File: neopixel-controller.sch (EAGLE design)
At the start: 22 parts, among them Q1 BSS138, Q2 BSS138, U1 ESP-WROOM-02, U2 AP2112K

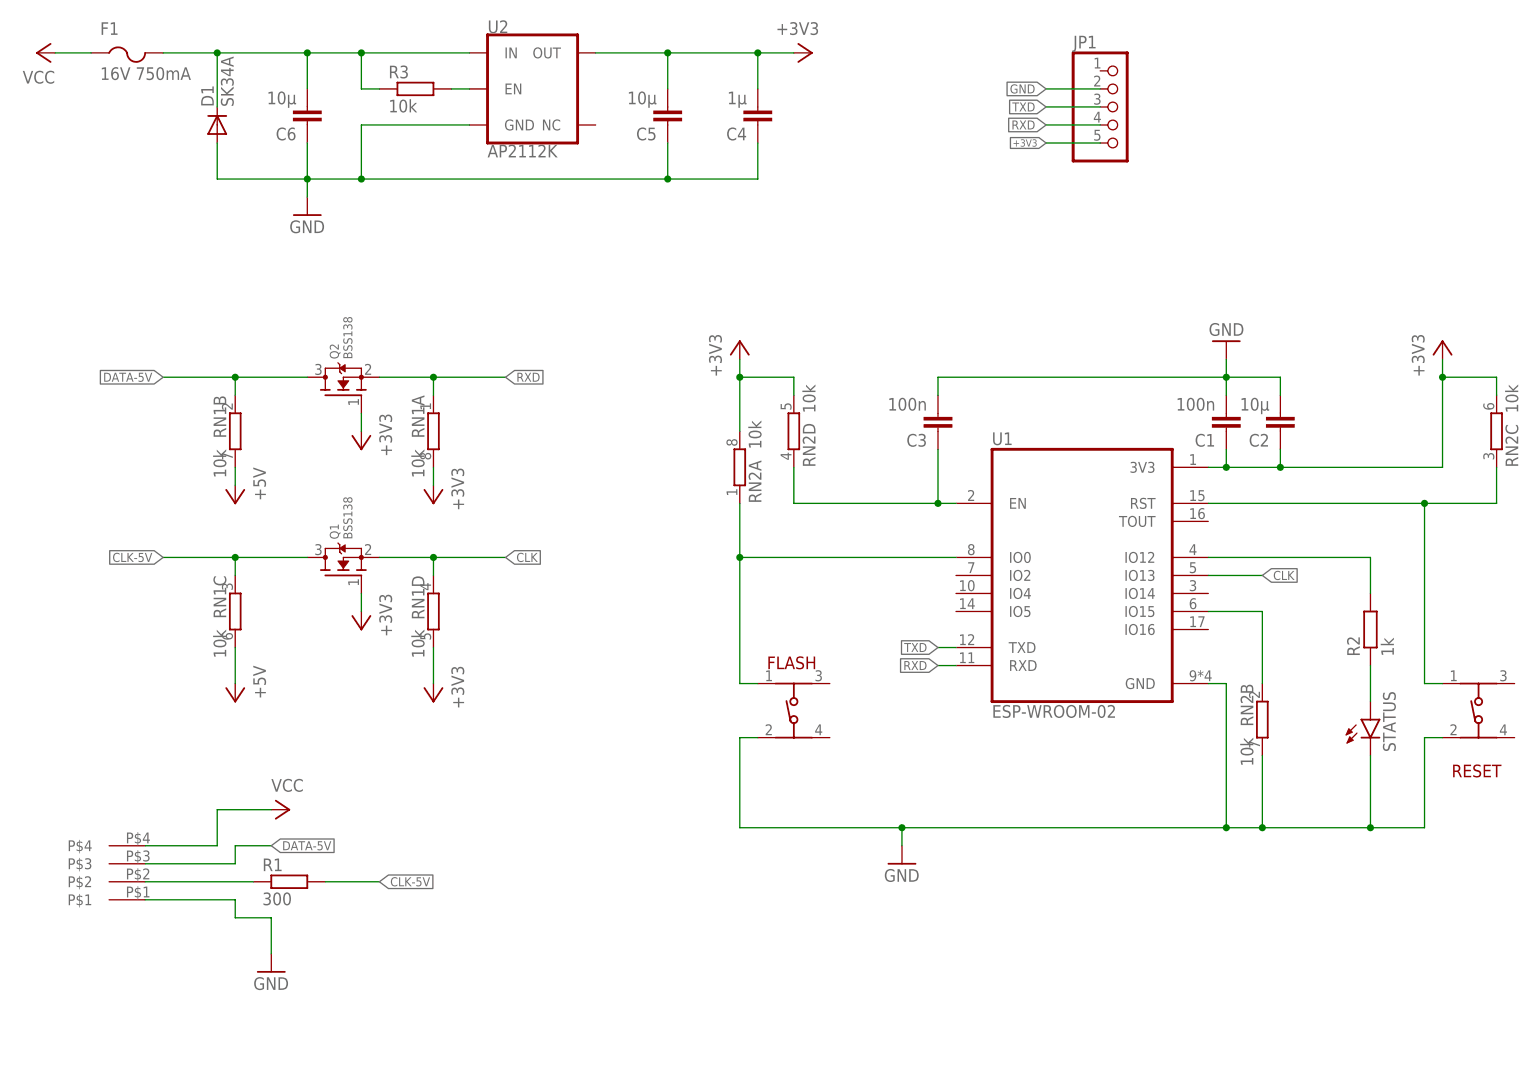
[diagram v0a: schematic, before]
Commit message: added 74ahct125, rework for v0.5
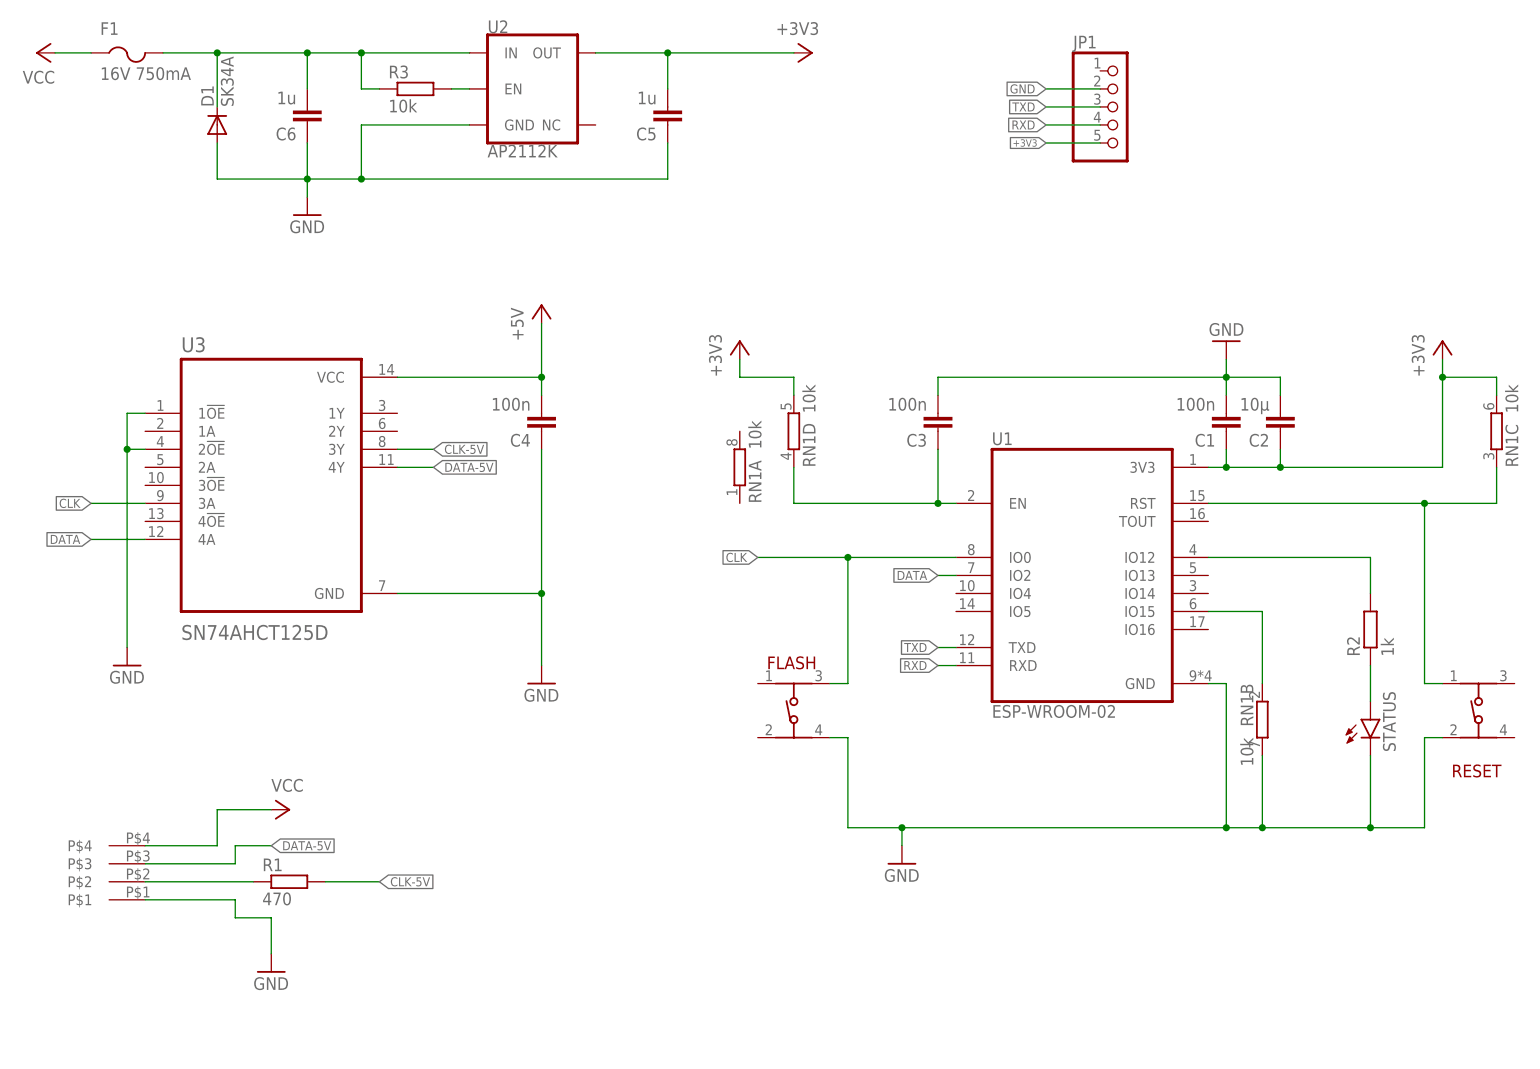
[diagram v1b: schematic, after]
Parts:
- removed Q1, Q2: BSS138, adafruit:MOSFET-NREFLOW
- removed RN2: 10k, resistor-dil:4R-NEXB38V
- added U3: SN74AHCT125D, SN74AHCT125D:SN74AHCT125D
- C4: value 1µ -> 100n
- C5, C6: value 10µ -> 1u
- R1: value 300 -> 470
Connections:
- removed net FLASH: FLASH.1, RN2A.1, U1.IO0
- new net DATA: U1.IO2, U3.4A
- net +3V3: now also RN1C.2; no longer C4.2, Q1.G, Q2.G, RN1A.2, RN2A.2, RN2C.2, RN2D.2
- net +5V: now also C4.2, U3.VCC; no longer RN1B.2, RN1C.2
- net BOOTMODE: now also RN1B.1; no longer RN2B.1
- net CHIPEN: now also RN1D.1; no longer RN2D.1
- net CLK: now also FLASH.2, U1.IO0, U3.3A; no longer Q1.S, RN1D.1, U1.IO13
- net CLK-5V: now also U3.3Y; no longer Q1.D, RN1C.1
- net DATA-5V: now also U3.4Y; no longer Q2.D, RN1B.1
- net GND: now also FLASH.4, RN1B.2, U3.1!OE, U3.2!OE, U3.GND; no longer FLASH.3, RN2B.2
- net RST: now also RN1C.1; no longer RN2C.1
- net RXD: no longer Q2.S, RN1A.1
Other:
- moved on the sheet: C4, RN1A, RN1B, RN1C, RN1D

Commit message: v0.5 pr
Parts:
- F1: value 16V 750mA -> 8V 500mA
- R1: value 470 -> 330
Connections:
- removed net N$3: R1.1, U$101.P$2
- new net DATA-5VR: R1.1, U$101.P$3
- net CLK-5V: now also U$101.P$2; no longer R1.2
- net DATA-5V: now also R1.2; no longer U$101.P$3
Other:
- moved on the sheet: R1
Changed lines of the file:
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@@
 <part name="JP1" library="pinhead" library_urn="urn:adsk.eagle:library:325" deviceset="PINHD-1X5" device="" package3d_urn="urn:adsk.eagle:package:22469/2"/>
 <part name="GND1" library="supply1" deviceset="GND" device=""/>
-<part name="R1" library="rcl" library_urn="urn:adsk.eagle:library:334" deviceset="R-EU_" device="R0805" package3d_urn="urn:adsk.eagle:package:23553/2" value="470"/>
+<part name="R1" library="rcl" library_urn="urn:adsk.eagle:library:334" deviceset="R-EU_" device="R0805" package3d_urn="urn:adsk.eagle:package:23553/2" value="330"/>
 <part name="FRAME1" library="frames" library_urn="urn:adsk.eagle:library:229" deviceset="A4L-LOC" device=""/>
 <part name="FLASH" library="434153017835_Eagle_WS-TASV_rev20a" deviceset="434153017835" device="" package3d_urn="urn:adsk.eagle:package:18304352/2"/>
@@
 <part name="D1" library="diode" library_urn="urn:adsk.eagle:library:210" deviceset="DIODE-" device="DO214AC" package3d_urn="urn:adsk.eagle:package:43417/2" value="SK34A"/>
 <part name="P+1" library="supply1" library_urn="urn:adsk.eagle:library:371" deviceset="VCC" device=""/>
-<part name="F1" library="adafruit" library_urn="urn:adsk.eagle:library:420" deviceset="PTCFUSE" device="-1206" package3d_urn="urn:adsk.eagle:package:6240569/1" override_package3d_urn="urn:adsk.eagle:package:20945049/2" override_package_urn="urn:adsk.eagle:footprint:6239923/1" value="16V 750mA"/>
+<part name="F1" library="adafruit" library_urn="urn:adsk.eagle:library:420" deviceset="PTCFUSE" device="-1206" package3d_urn="urn:adsk.eagle:package:6240569/1" override_package3d_urn="urn:adsk.eagle:package:20945049/2" override_package_urn="urn:adsk.eagle:footprint:6239923/1" value="8V 500mA"/>
 <part name="RN1" library="resistor-dil" library_urn="urn:adsk.eagle:library:342" deviceset="4R-N" device="EXB38V" package3d_urn="urn:adsk.eagle:package:24923/1" override_package3d_urn="urn:adsk.eagle:package:20945039/2" override_package_urn="urn:adsk.eagle:footprint:24902/1" value="10k"/>
 <part name="U3" library="SN74AHCT125D" deviceset="SN74AHCT125D" device="" override_package3d_urn="urn:adsk.eagle:package:23111573/2" override_package_urn="urn:adsk.eagle:footprint:23111574/1"/>
@@
 <attribute name="VALUE" x="149.86" y="35.56" size="1.778" layer="96"/>
 </instance>
-<instance part="+3V35" gate="G$1" x="129.54" y="111.76" smashed="yes">
-<attribute name="VALUE" x="127" y="106.68" size="1.778" layer="96" rot="R90"/>
+<instance part="+3V35" gate="G$1" x="137.16" y="111.76" smashed="yes">
+<attribute name="VALUE" x="134.62" y="106.68" size="1.778" layer="96" rot="R90"/>
 </instance>
 <instance part="+3V37" gate="G$1" x="228.6" y="111.76" smashed="yes">
@@
 <attribute name="VALUE" x="60.96" y="20.32" size="1.778" layer="96"/>
 </instance>
-<instance part="R1" gate="G$1" x="66.04" y="35.56" smashed="yes">
-<attribute name="NAME" x="62.23" y="37.0586" size="1.778" layer="95"/>
-<attribute name="VALUE" x="62.23" y="32.258" size="1.778" layer="96"/>
+<instance part="R1" gate="G$1" x="68.58" y="40.64" smashed="yes">
+<attribute name="NAME" x="64.77" y="42.1386" size="1.778" layer="95"/>
+<attribute name="VALUE" x="64.77" y="37.338" size="1.778" layer="96"/>
 </instance>
 <instance part="FRAME1" gate="G$1" x="0" y="0" smashed="yes">
@@
 <segment>
 <pinref part="+3V35" gate="G$1" pin="+3V3"/>
-<wire x1="129.54" y1="106.68" x2="129.54" y2="109.22" width="0.1524" layer="91"/>
-<wire x1="137.16" y1="104.14" x2="137.16" y2="106.68" width="0.1524" layer="91"/>
-<wire x1="137.16" y1="106.68" x2="129.54" y2="106.68" width="0.1524" layer="91"/>
+<wire x1="137.16" y1="104.14" x2="137.16" y2="109.22" width="0.1524" layer="91"/>
 <pinref part="RN1" gate="D" pin="2"/>
 </segment>
@@
 <net name="DATA-5V" class="0">
 <segment>
-<wire x1="58.42" y1="40.64" x2="63.5" y2="40.64" width="0.1524" layer="91"/>
-<label x="63.5" y="40.64" size="1.27" layer="95" xref="yes"/>
-<pinref part="U$101" gate="G$1" pin="P$3"/>
-<wire x1="45.72" y1="38.1" x2="58.42" y2="38.1" width="0.1524" layer="91"/>
-<wire x1="58.42" y1="38.1" x2="58.42" y2="40.64" width="0.1524" layer="91"/>
-</segment>
-<segment>
 <label x="86.36" y="93.98" size="1.27" layer="95" xref="yes"/>
 <pinref part="U3" gate="G$1" pin="4Y"/>
 <wire x1="81.28" y1="93.98" x2="86.36" y2="93.98" width="0.1524" layer="91"/>
+</segment>
+<segment>
+<wire x1="73.66" y1="40.64" x2="78.74" y2="40.64" width="0.1524" layer="91"/>
+<label x="78.74" y="40.64" size="1.27" layer="95" xref="yes"/>
+<pinref part="R1" gate="G$1" pin="2"/>
 </segment>
 </net>
@@
 </segment>
 <segment>
-<pinref part="R1" gate="G$1" pin="2"/>
-<wire x1="71.12" y1="35.56" x2="78.74" y2="35.56" width="0.1524" layer="91"/>
-<label x="78.74" y="35.56" size="1.27" layer="95" xref="yes"/>
+<label x="76.2" y="35.56" size="1.27" layer="95" xref="yes"/>
+<pinref part="U$101" gate="G$1" pin="P$2"/>
+<wire x1="45.72" y1="35.56" x2="76.2" y2="35.56" width="0.1524" layer="91"/>
 </segment>
 </net>
@@
 </segment>
 </net>
-<net name="N$3" class="0">
-<segment>
-<pinref part="U$101" gate="G$1" pin="P$2"/>
-<pinref part="R1" gate="G$1" pin="1"/>
-<wire x1="45.72" y1="35.56" x2="60.96" y2="35.56" width="0.1524" layer="91"/>
-</segment>
-</net>
 <net name="DATA" class="0">
 <segment>
@@
 </segment>
 </net>
+<net name="DATA-5VR" class="0">
+<segment>
+<pinref part="U$101" gate="G$1" pin="P$3"/>
+<wire x1="45.72" y1="38.1" x2="60.96" y2="38.1" width="0.1524" layer="91"/>
+<wire x1="60.96" y1="38.1" x2="60.96" y2="40.64" width="0.1524" layer="91"/>
+<pinref part="R1" gate="G$1" pin="1"/>
+<wire x1="60.96" y1="40.64" x2="63.5" y2="40.64" width="0.1524" layer="91"/>
+</segment>
+</net>

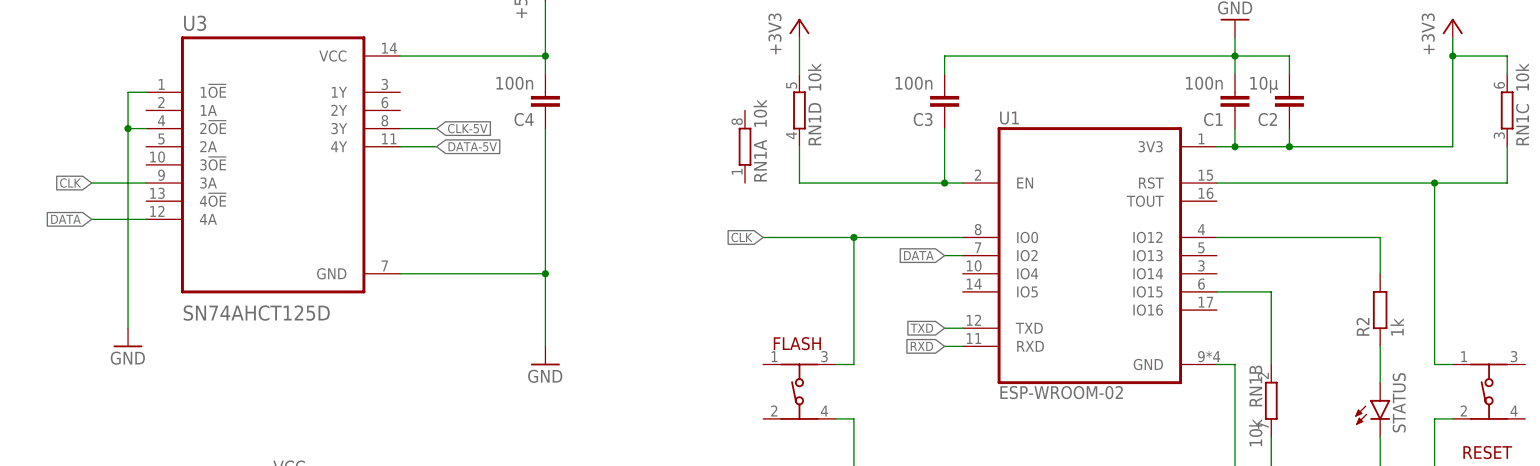
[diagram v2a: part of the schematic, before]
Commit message: fixed OE of 74AHCT125
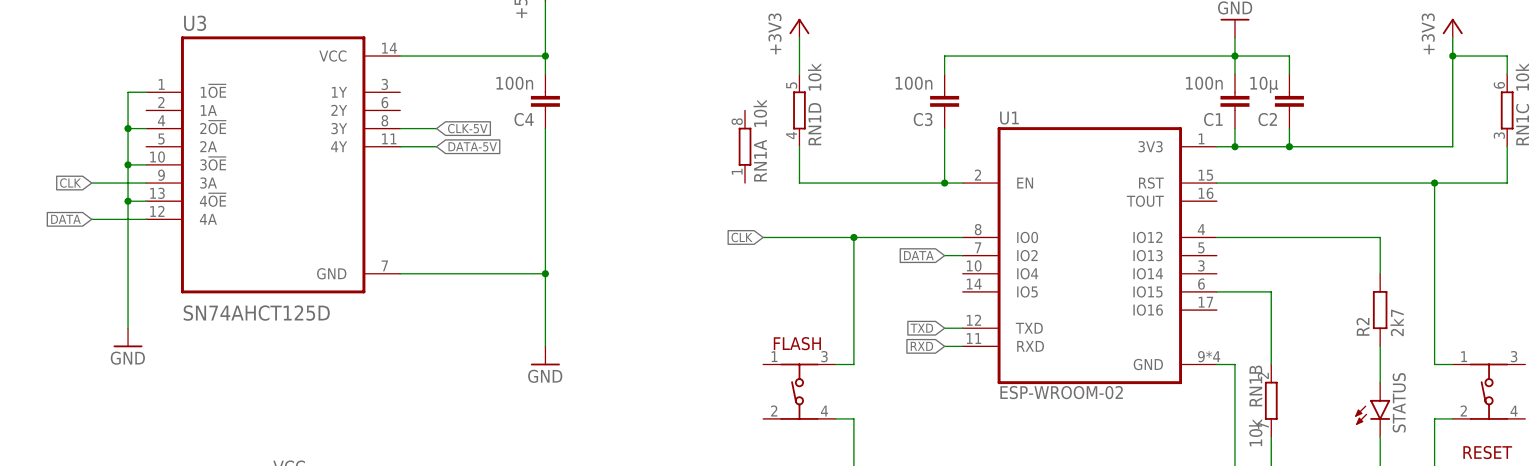
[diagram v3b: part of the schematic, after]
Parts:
- R2: value 1k -> 2k7
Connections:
- net GND: now also U3.3!OE, U3.4!OE
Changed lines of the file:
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@@
 <part name="C3" library="rcl" library_urn="urn:adsk.eagle:library:334" deviceset="C-EU" device="C0805" package3d_urn="urn:adsk.eagle:package:23617/2" value="100n"/>
 <part name="U1" library="ESP-WROOM-02" deviceset="ESP-WROOM-02" device="" override_package3d_urn="urn:adsk.eagle:package:14797501/2" override_package_urn="urn:adsk.eagle:footprint:14797502/1" override_locally_modified="yes"/>
-<part name="R2" library="rcl" library_urn="urn:adsk.eagle:library:334" deviceset="R-EU_" device="R0805" package3d_urn="urn:adsk.eagle:package:23553/2" value="1k"/>
+<part name="R2" library="rcl" library_urn="urn:adsk.eagle:library:334" deviceset="R-EU_" device="R0805" package3d_urn="urn:adsk.eagle:package:23553/2" value="2k7"/>
 <part name="STATUS" library="led" library_urn="urn:adsk.eagle:library:259" deviceset="LED" device="CHIPLED_0805" package3d_urn="urn:adsk.eagle:package:15821/2"/>
 <part name="JP1" library="pinhead" library_urn="urn:adsk.eagle:library:325" deviceset="PINHD-1X5" device="" package3d_urn="urn:adsk.eagle:package:22469/2"/>
@@
 <wire x1="43.18" y1="101.6" x2="43.18" y2="96.52" width="0.1524" layer="91"/>
 <pinref part="U3" gate="G$1" pin="2!OE"/>
-<wire x1="43.18" y1="96.52" x2="43.18" y2="68.58" width="0.1524" layer="91"/>
+<wire x1="43.18" y1="96.52" x2="43.18" y2="91.44" width="0.1524" layer="91"/>
+<wire x1="43.18" y1="91.44" x2="43.18" y2="86.36" width="0.1524" layer="91"/>
+<wire x1="43.18" y1="86.36" x2="43.18" y2="68.58" width="0.1524" layer="91"/>
 <wire x1="45.72" y1="96.52" x2="43.18" y2="96.52" width="0.1524" layer="91"/>
 <junction x="43.18" y="96.52"/>
-</segment>
-<segment>
+<pinref part="U3" gate="G$1" pin="3!OE"/>
+<wire x1="45.72" y1="91.44" x2="43.18" y2="91.44" width="0.1524" layer="91"/>
+<junction x="43.18" y="91.44"/>
+<pinref part="U3" gate="G$1" pin="4!OE"/>
+<wire x1="45.72" y1="86.36" x2="43.18" y2="86.36" width="0.1524" layer="91"/>
+<junction x="43.18" y="86.36"/>
+</segment>
+<segment>

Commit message: minor changes in schematic
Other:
- note added: "WLAN Pixel Controller V0.6 codm.de, 2020 CC-BY-NC-SA"
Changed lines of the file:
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@@
 <sheet>
 <plain>
+<text x="162.56" y="12.7" size="2.54" layer="94" font="vector">WLAN Pixel Controller V0.6
+codm.de, 2020
+CC-BY-NC-SA</text>
 </plain>
 <instances>
@@
 </drawing>
 <compatibility>
+<note version="6.3" minversion="6.2.2" severity="warning">
+Since Version 6.2.2 text objects can contain more than one line,
+which will not be processed correctly with this version.
+</note>
 <note version="8.2" severity="warning">
 Since Version 8.2, EAGLE supports online libraries. The ids
